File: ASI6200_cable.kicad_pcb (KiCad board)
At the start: 2 copper layers, 105.1 x 25.5 mm, 2 parts, among them J1 TF31-50S-0.5SH_800_, J2 TF31-50S-0.5SH_800_

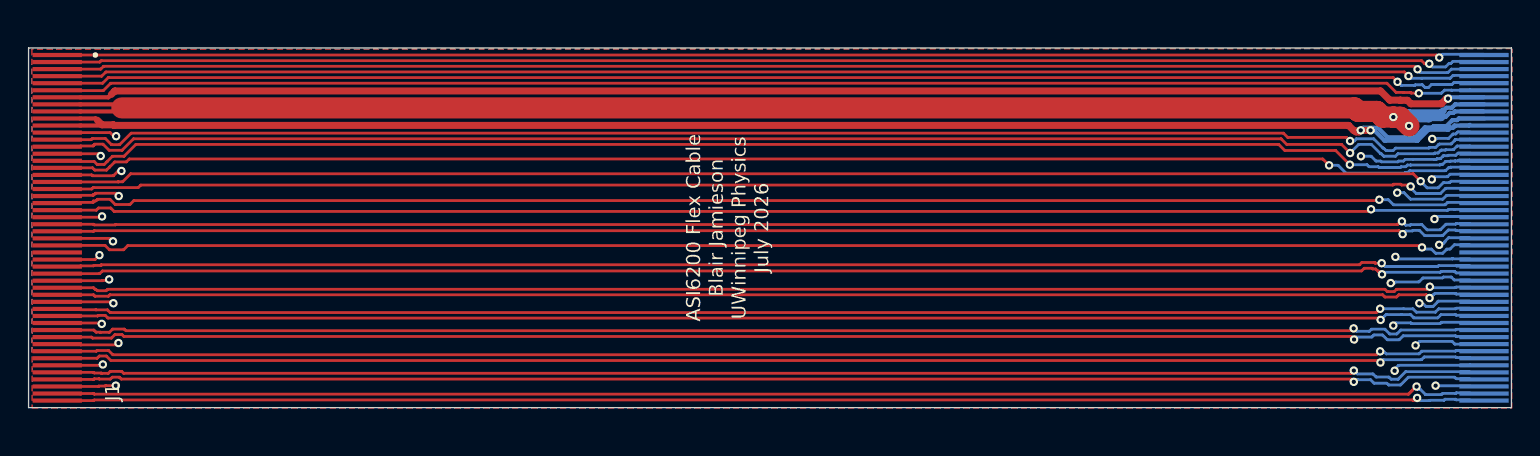
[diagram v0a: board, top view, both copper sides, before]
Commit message: Update FFC for same-side ASI6200 cameras
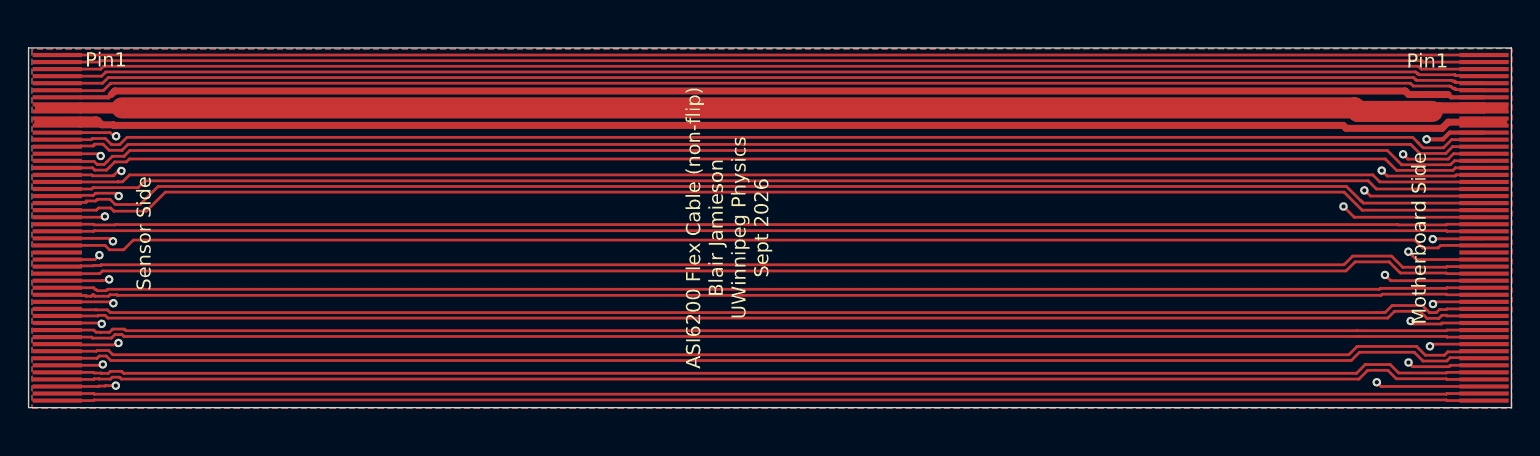
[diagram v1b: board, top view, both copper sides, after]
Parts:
- J2: moved to F.Cu
- turned J2 to 90 degrees
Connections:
- J2 pad 1: /DQ0_P -> /SPI_CS
- J2 pad 10: /DQ3_P -> +5V
- J2 pad 11: /DQ3_N -> +5V
- J2 pad 13: /DQ4_P -> /I2C_SDA
- J2 pad 14: /DQ4_N -> /I2C_SCL
- J2 pad 16: /DQ5_P -> /VAA12_EN
- J2 pad 17: /DQ5_N -> /HOT_CONTROL
- J2 pad 19: /DQ6_P -> /VAA18_EN
- J2 pad 2: /DQ0_N -> /SPI_CLK
- J2 pad 20: /DQ6_N -> /XPI
- J2 pad 22: unconnected-(J2-Pad22) -> /LONG_EXP_EN
- J2 pad 23: /SYNC_CLK_OUT -> /AVDD_PWR_EN
- J2 pad 25: /DQ7_P -> /DQ7_N
- J2 pad 26: /DQ7_N -> /DQ7_P
- J2 pad 28: /AVDD_PWR_EN -> /SYNC_CLK_OUT
- J2 pad 29: /LONG_EXP_EN -> unconnected-(J2-Pad29)
- J2 pad 3: GND -> /SPI_SDA
- J2 pad 31: /XPI -> /DQ6_N
- J2 pad 32: /VAA18_EN -> /DQ6_P
- J2 pad 34: /HOT_CONTROL -> /DQ5_N
- J2 pad 35: /VAA12_EN -> /DQ5_P
- J2 pad 37: /I2C_SCL -> /DQ4_N
- J2 pad 38: /I2C_SDA -> /DQ4_P
- J2 pad 4: /DQ1_P -> /SPI_SDO
- J2 pad 40: +5V -> /DQ3_N
- J2 pad 41: +5V -> /DQ3_P
- J2 pad 42: +1V8 -> GND
- J2 pad 43: +1V8 -> /DQ2_N
- J2 pad 44: +12V -> /DQ2_P
- J2 pad 45: /Sensor_XHS -> GND
- J2 pad 46: /Sensor_XVS -> /DQ1_N
- J2 pad 47: /SPI_SDO -> /DQ1_P
- J2 pad 48: /SPI_SDA -> GND
- J2 pad 49: /SPI_CLK -> /DQ0_N
- J2 pad 5: /DQ1_N -> /Sensor_XVS
- J2 pad 50: /SPI_CS -> /DQ0_P
- J2 pad 6: GND -> /Sensor_XHS
- J2 pad 7: /DQ2_P -> +12V
- J2 pad 8: /DQ2_N -> +1V8
- J2 pad 9: GND -> +1V8
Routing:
- net GND: track 86.5 -> 109.0 mm
- net +1V8: track 110.5 -> 118.4 mm, vias 2 -> 0
- net +5V: track 111.0 -> 107.3 mm, vias 2 -> 0
- net /AVDD_PWR_EN: track 98.9 -> 102.4 mm, vias 1 -> 0
- net /LONG_EXP_EN: track 99.4 -> 100.9 mm, vias 1 -> 0
- net /DQ2_P: track 99.0 -> 100.4 mm, vias 1 -> 0
- net /DQ2_N: track 99.0 -> 100.3 mm, vias 1 -> 0
- net /DQ4_N: track 99.0 -> 100.2 mm, vias 1 -> 0
- net /DQ4_P: track 99.1 -> 100.2 mm, vias 1 -> 0
- net /SYNC_CLK_OUT: track 99.3 -> 100.3 mm, vias 1 -> 0
- net /DQ1_N: track 99.3 -> 100.2 mm, vias 1 -> 0
- net /DQ1_P: track 99.3 -> 100.2 mm, vias 1 -> 0
- net /SPI_SDO: track 98.9 -> 99.8 mm, vias 1 -> 0
- net /Sensor_XHS: track 99.2 -> 100.0 mm, vias 1 -> 0
- net /DQ5_P: track 99.0 -> 99.8 mm, vias 1 -> 0
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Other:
- board text added: "ASI6200 Flex Cable (non-flip) Blair Jamieson UWinnipeg Physics Sept 2026"
- board text added: "Motherboard Side"
- board text added: "Pin1"
- board text added: "Sensor Side"
- board text removed: "ASI6200 Flex Cable Blair Jamieson UWinnipeg Physics July 2026"
